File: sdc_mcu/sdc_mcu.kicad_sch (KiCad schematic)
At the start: 141 parts, among them J3 USB_C_Receptacle_USB2.0_16P, J4 Conn_01x03_Pin, J5 Conn_01x02_Pin, J6 Conn_01x02_Pin, J7 Conn_02x15_Odd_Even, K1 G2RL-2A, K2 G2RL-2A, K3 G2RL-2A, K4 G2RL-2A, Q1 2N7002, Q2 2N7002, Q3 2N7002, Q4 2N7002, Q5 2N7002, Q6 2N7002, Q7 2N7002, Q9 Si2301CDS, SW1 SW_SPST, U1 VOM618AT, U10 AP2204K-ADJ, U11 STM32F103C8Tx, U12 AP2204K-ADJ, U2 VOM618AT, U3 AS331KTR-G1, U4 AS331KTR-G1, U5 AS331KTR-G1, U6 VOM618AT, U7 VOM618AT, U8 SN65HVD256D, U9 AP2204K-ADJ, Y1 8M, Y2 32.768k

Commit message: v2025.10
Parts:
- removed D15: ~, LED_SMD:LED_0805_2012Metric, symbol Device:LED_Small
- removed Q9: Si2301CDS, Package_TO_SOT_SMD:SOT-23, symbol Transistor_FET:Si2319CDS
- removed R60: 4.7k, Resistor_SMD:R_0603_1608Metric, symbol Device:R
- added D15: LED, LED_SMD:LED_0805_2012Metric, symbol Device:LED
- added D16, D17, D18: ~, LED_SMD:LED_0805_2012Metric, symbol Device:LED_Small
- added J1: Conn_02x05_Odd_Even, Connector_PinHeader_2.54mm:PinHeader_2x05_P2.54mm_Vertical, symbol Connector_Generic:Conn_02x05_Odd_Even
- added JP2: Jumper_2_Open, Connector_PinHeader_2.54mm:PinHeader_1x02_P2.54mm_Vertical, symbol Jumper:Jumper_2_Open
- added Q8: 2N7002, Package_TO_SOT_SMD:SOT-23, symbol Transistor_FET:2N7002
- added R60, R61, R62, R63: 10k, Resistor_SMD:R_0603_1608Metric, symbol Device:R_Small
- C23: value 1u -> 10u; footprint Capacitor_SMD:C_0603_1608Metric -> Capacitor_SMD:C_0805_2012Metric
- J4: footprint (none) -> Connector_PinHeader_2.54mm:PinHeader_1x03_P2.54mm_Vertical
- J5, J6: footprint (none) -> Connector_PinHeader_2.54mm:PinHeader_1x02_P2.54mm_Vertical
- J7: footprint (none) -> Connector_PinHeader_2.54mm:PinHeader_2x15_P2.54mm_Vertical
- R18, R19, R59: value 1k -> 10k
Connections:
- net +3.3V: now also R60.1
- net BMS_FAULT: now also J7.15 (Pin_15); no longer J7.21 (Pin_21)
- net BMS_FAULT_OUT: now also R62.1
- net BMS_LED: now also J7.14 (Pin_14); no longer J7.22 (Pin_22)
- net BMS_RST: now also J7.16 (Pin_16); no longer J7.20 (Pin_20)
- net BSPD_FAULT: now also J7.22 (Pin_22); no longer J7.15 (Pin_15)
- net BSPD_FAULT_OUT: now also R61.1
- net BSPD_IN: now also J7.28 (Pin_28); no longer J7.14 (Pin_14)
- net BSPD_LED: now also J7.23 (Pin_23); no longer J7.11 (Pin_11)
- net BSPD_RST: now also J7.21 (Pin_21); no longer J7.13 (Pin_13)
- net BSPD_signal1: now also J7.7 (Pin_7); no longer J7.8 (Pin_8)
- net BSPD_signal2: now also J7.8 (Pin_8); no longer J7.7 (Pin_7)
- net BSPD_signal3: now also J7.9 (Pin_9); no longer J7.10 (Pin_10)
- net BSPD_signal4: now also J7.10 (Pin_10); no longer J7.9 (Pin_9)
- net CAN+: now also J7.2 (Pin_2), JP2.2 (B); no longer J7.3 (Pin_3), R37.1
- net CAN-: now also J7.3 (Pin_3); no longer J7.2 (Pin_2)
- net GND: now also J7.11 (Pin_11), J7.24 (Pin_24), J7.26 (Pin_26), J7.30 (Pin_30), J7.6 (Pin_6), D16.1 (K), D17.1 (K), D18.1 (K), J1.1 (Pin_1), J1.9 (Pin_9), Q8.2 (S); no longer J7.16 (Pin_16), J7.23 (Pin_23), J7.25 (Pin_25), J7.29 (Pin_29), J7.5 (Pin_5)
- net IMD_FAULT: now also J7.17 (Pin_17); no longer J7.18 (Pin_18)
- net IMD_FAULT_OUT: now also R63.1
- net IMD_LED: now also J7.20 (Pin_20); no longer J7.17 (Pin_17)
- net IMD_RST: now also J7.18 (Pin_18); no longer J7.19 (Pin_19)
- net SDC_OUT: now also J7.13 (Pin_13); no longer J7.27 (Pin_27)
- net SWDIO: now also Q8.1 (G)
- net SW_Fault: now also J7.19 (Pin_19); no longer J7.24 (Pin_24)
- net TSSI: now also J7.5 (Pin_5); no longer J7.6 (Pin_6)
- net VDC: now also J7.27 (Pin_27), J7.29 (Pin_29); no longer J7.28 (Pin_28), J7.30 (Pin_30)
- net PB11: now reaches U11.22 (PB11)
- net PB11: now also J1.2 (Pin_2)
- net PB12: now reaches U11.25 (PB12)
- net PB12: now also J1.4 (Pin_4)
- net PB13: now reaches U11.26 (PB13)
- net PB13: now also J1.6 (Pin_6)
- net PB14: now reaches U11.27 (PB14)
- net PB14: now also J1.8 (Pin_8)
- net PB15: now reaches U11.28 (PB15)
- net PB15: now also J1.10 (Pin_10)
- net PA8: now reaches U11.29 (PA8)
- net PA8: now also J1.3 (Pin_3)
- net PA9: now reaches U11.30 (PA9)
- net PA9: now also J1.7 (Pin_7)
- net PA10: now reaches U11.31 (PA10)
- net PA10: now also J1.5 (Pin_5)
- net NRST: no longer names the net of R58.2, SW1.2 (B), U11.7 (NRST)
- new net: D15.2 (A), R60.2
- new net: JP2.1 (A), R37.1
- new net: D15.1 (K), Q8.3 (D)
- new net: D16.2 (A), R61.2
- new net: D17.2 (A), R62.2
- new net: D18.2 (A), R63.2
- no-connect marks 21 -> 13
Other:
- moved on the sheet: C18, C19, C20, C21, U8, Y1, Y2

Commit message: feat: relayout sdc mcu
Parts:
- removed C14: 1u, Capacitor_SMD:C_0603_1608Metric_Pad1.08x0.95mm_HandSolder, symbol Device:C_Small
- removed C15: 10u, Capacitor_SMD:C_0805_2012Metric_Pad1.18x1.45mm_HandSolder, symbol Device:C_Small
- removed D14: BAT46W-7-F, Diode_SMD:D_SOD-123, symbol Diode:1N4148W
- removed D8: PWR, LED_SMD:LED_0805_2012Metric, symbol Device:LED_Small
- removed J1: Conn_02x05_Odd_Even, Connector_PinHeader_2.54mm:PinHeader_2x05_P2.54mm_Vertical, symbol Connector_Generic:Conn_02x05_Odd_Even
- removed J3: USB_C_Receptacle_USB2.0_16P, Connector_USB:USB_C_Receptacle_HRO_TYPE-C-31-M-12, symbol Connector:USB_C_Receptacle_USB2.0_16P
- removed J6: Conn_01x02_Pin, Connector_PinHeader_2.54mm:PinHeader_1x02_P2.54mm_Vertical, symbol Connector:Conn_01x02_Pin
- removed J7: Conn_02x15_Odd_Even, Connector_PinHeader_2.54mm:PinHeader_2x15_P2.54mm_Vertical, symbol Connector_Generic:Conn_02x15_Odd_Even
- removed R18: 10k, Resistor_SMD:R_0603_1608Metric, symbol Device:R_Small
- removed R31: 866k, Resistor_SMD:R_0603_1608Metric, symbol Device:R_Small
- removed R32: 100k, Resistor_SMD:R_0603_1608Metric, symbol Device:R_Small
- removed R52, R53: 5k1, Resistor_SMD:R_0603_1608Metric, symbol Device:R_Small
- removed R58: 10k, Resistor_SMD:R_0603_1608Metric, symbol Device:R
- removed SW1: SW_SPST, Button_Switch_SMD:SW_SPST_FSMSM, symbol Switch:SW_SPST
- removed U9: AP2204K-ADJ, Package_TO_SOT_SMD:SOT-23-5, symbol Regulator_Linear:AP2204K-ADJ
- added D19: DESD2CAN2SOQ, Package_TO_SOT_SMD:TSOT-23, symbol Device:D_TVS_Dual_AAC
- added J2: Conn_02x13_Odd_Even, Connector_PinHeader_2.54mm:PinHeader_2x13_P2.54mm_Vertical, symbol Connector_Generic:Conn_02x13_Odd_Even
- JP2: footprint Connector_PinHeader_2.54mm:PinHeader_1x02_P2.54mm_Vertical -> TestPoint:TestPoint_2Pads_Pitch2.54mm_Drill0.8mm
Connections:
- net +12V: now also J2.23 (Pin_23)
- net BMS_FAULT: now also J2.11 (Pin_11)
- net BMS_LED: now also J2.10 (Pin_10)
- net BMS_RST: now also J2.12 (Pin_12)
- net BSPD_FAULT: now also J2.18 (Pin_18)
- net BSPD_IN: now also J2.24 (Pin_24)
- net BSPD_LED: now also J2.19 (Pin_19)
- net BSPD_RST: now also J2.17 (Pin_17)
- net BSPD_signal1: now also J2.3 (Pin_3)
- net BSPD_signal2: now also J2.4 (Pin_4)
- net BSPD_signal3: now also J2.5 (Pin_5)
- net BSPD_signal4: now also J2.6 (Pin_6)
- net CAN+: now also JP2.1 (A), D19.2 (A2), J2.26 (Pin_26); no longer JP2.2 (B)
- net CAN-: now also D19.1 (A1), J2.25 (Pin_25)
- net GND: now also D19.3 (common), J2.2 (Pin_2), J2.20 (Pin_20), J2.22 (Pin_22), J2.7 (Pin_7), J2.8 (Pin_8)
- net IMD_FAULT: now also J2.13 (Pin_13)
- net IMD_LED: now also J2.16 (Pin_16)
- net IMD_RST: now also J2.14 (Pin_14)
- net SDC_OUT: now also J2.9 (Pin_9)
- net SW_Fault: now also J2.15 (Pin_15)
- net TSSI: now also J2.1 (Pin_1)
- net at R37.1: now also JP2.2 (B); no longer JP2.1 (A)
- net +3.3V renamed +3V3
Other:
- note removed: "RESET circuit"
- moved on the sheet: C8, R37, R38

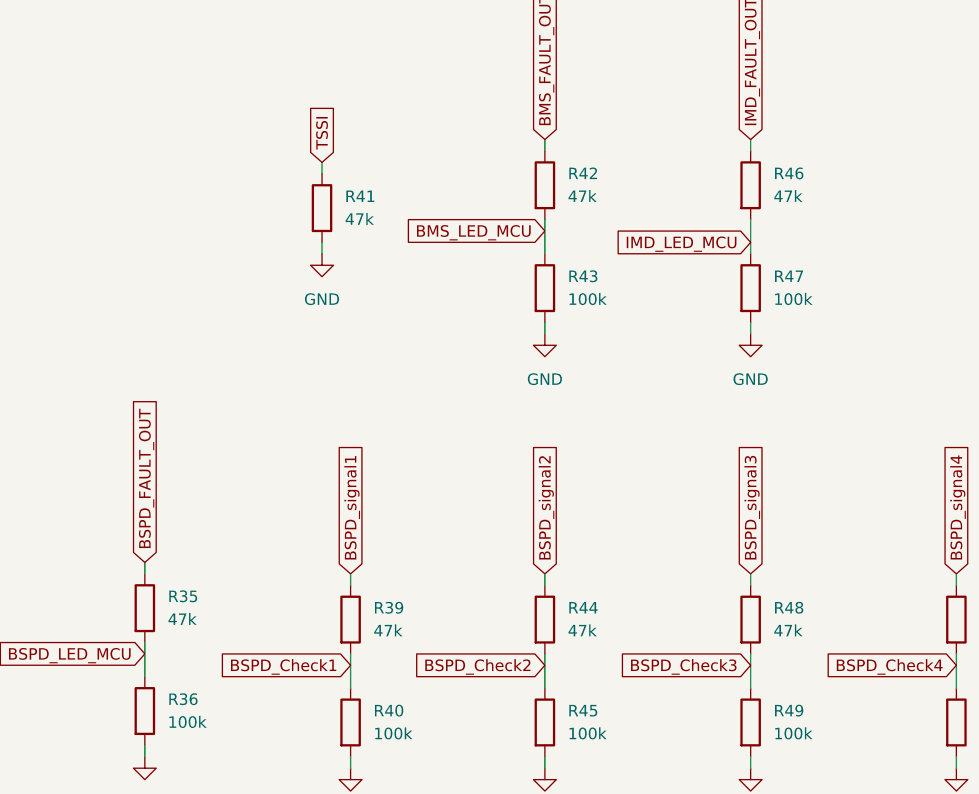
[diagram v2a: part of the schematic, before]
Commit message: fix: resistor of SDC_MCU
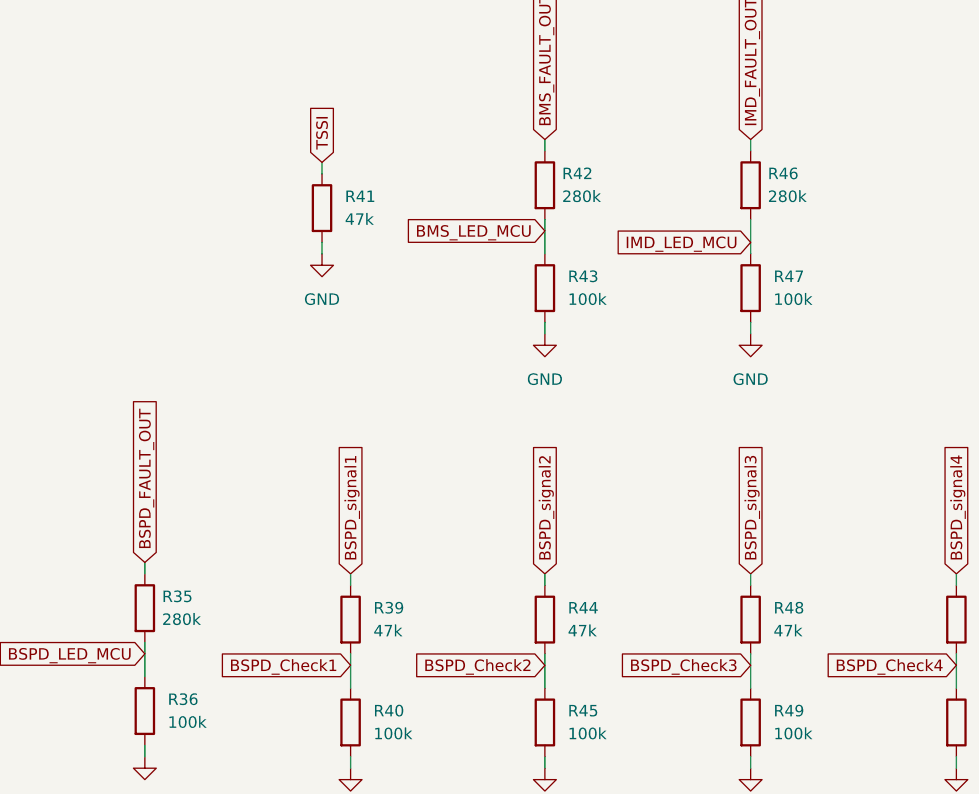
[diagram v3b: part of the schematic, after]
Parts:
- R35, R42, R46: value 47k -> 280k
